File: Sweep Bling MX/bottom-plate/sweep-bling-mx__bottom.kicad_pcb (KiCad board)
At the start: 2 copper layers, 113.5 x 95.2 mm, 8 parts

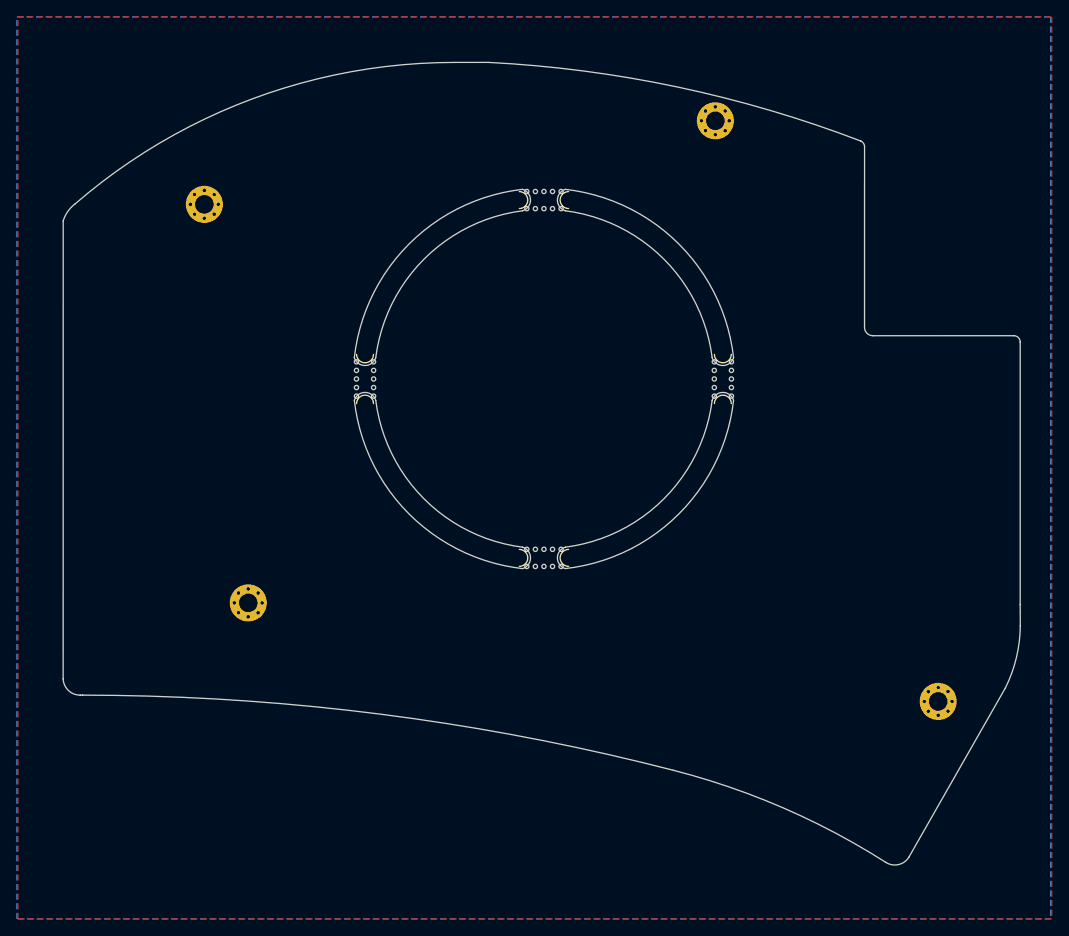
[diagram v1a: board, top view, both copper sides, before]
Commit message: Update bottom plate malformed edge cuts
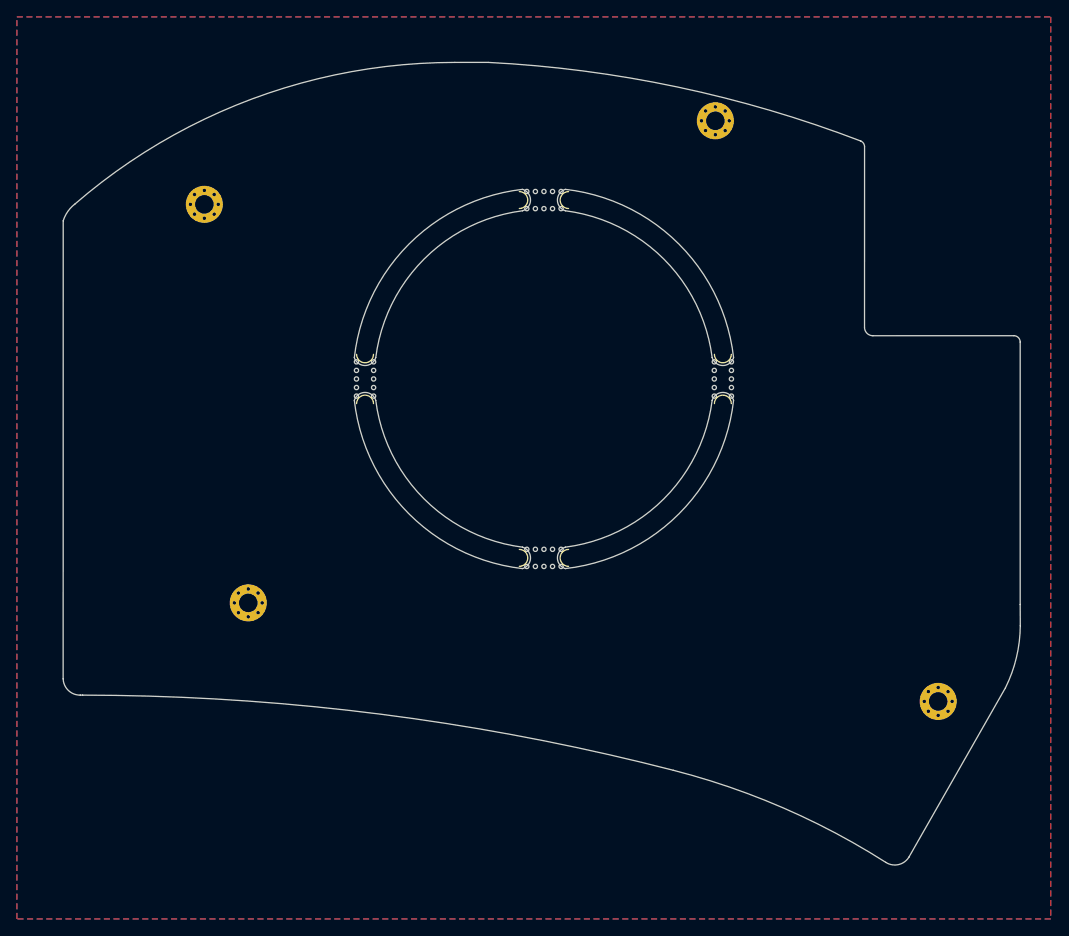
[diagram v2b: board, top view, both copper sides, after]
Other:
- board size 113.5 x 95.2 mm -> 113.5 x 95.1 mm
- net class Default removed
